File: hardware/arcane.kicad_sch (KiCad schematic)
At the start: 5 parts, among them J1 Conn_01x02, J2 Conn_01x07, SW1 SW_Push, U1 XIAO-nRF52840-SMD

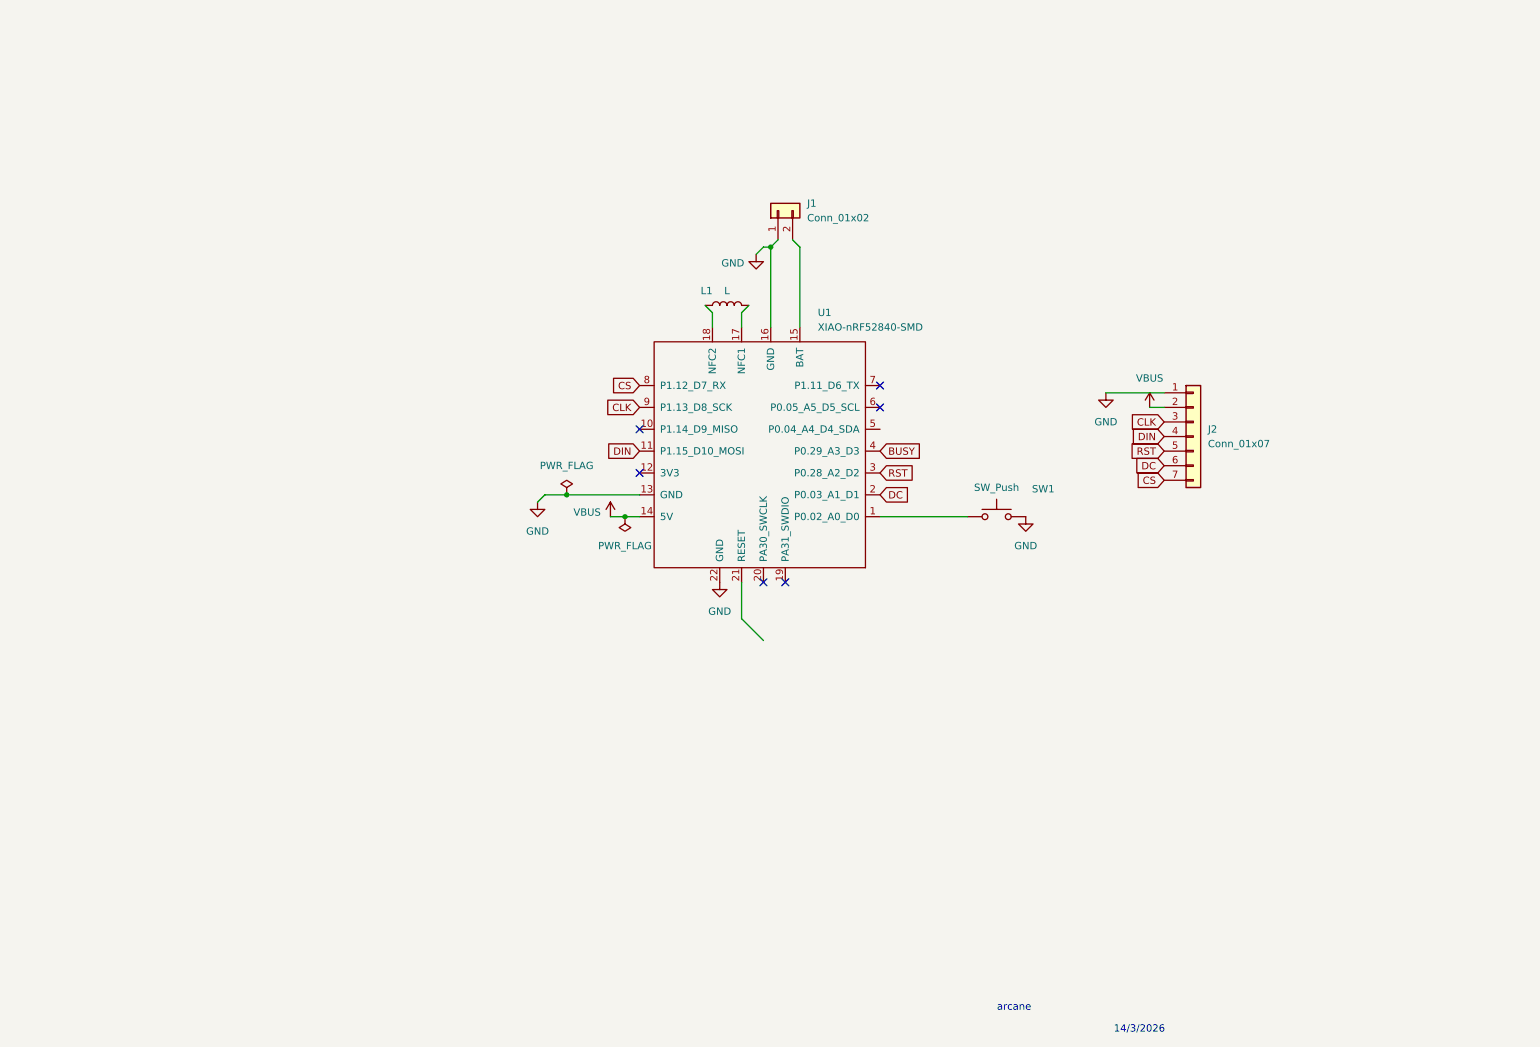
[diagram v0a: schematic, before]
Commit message: migrate to stm32
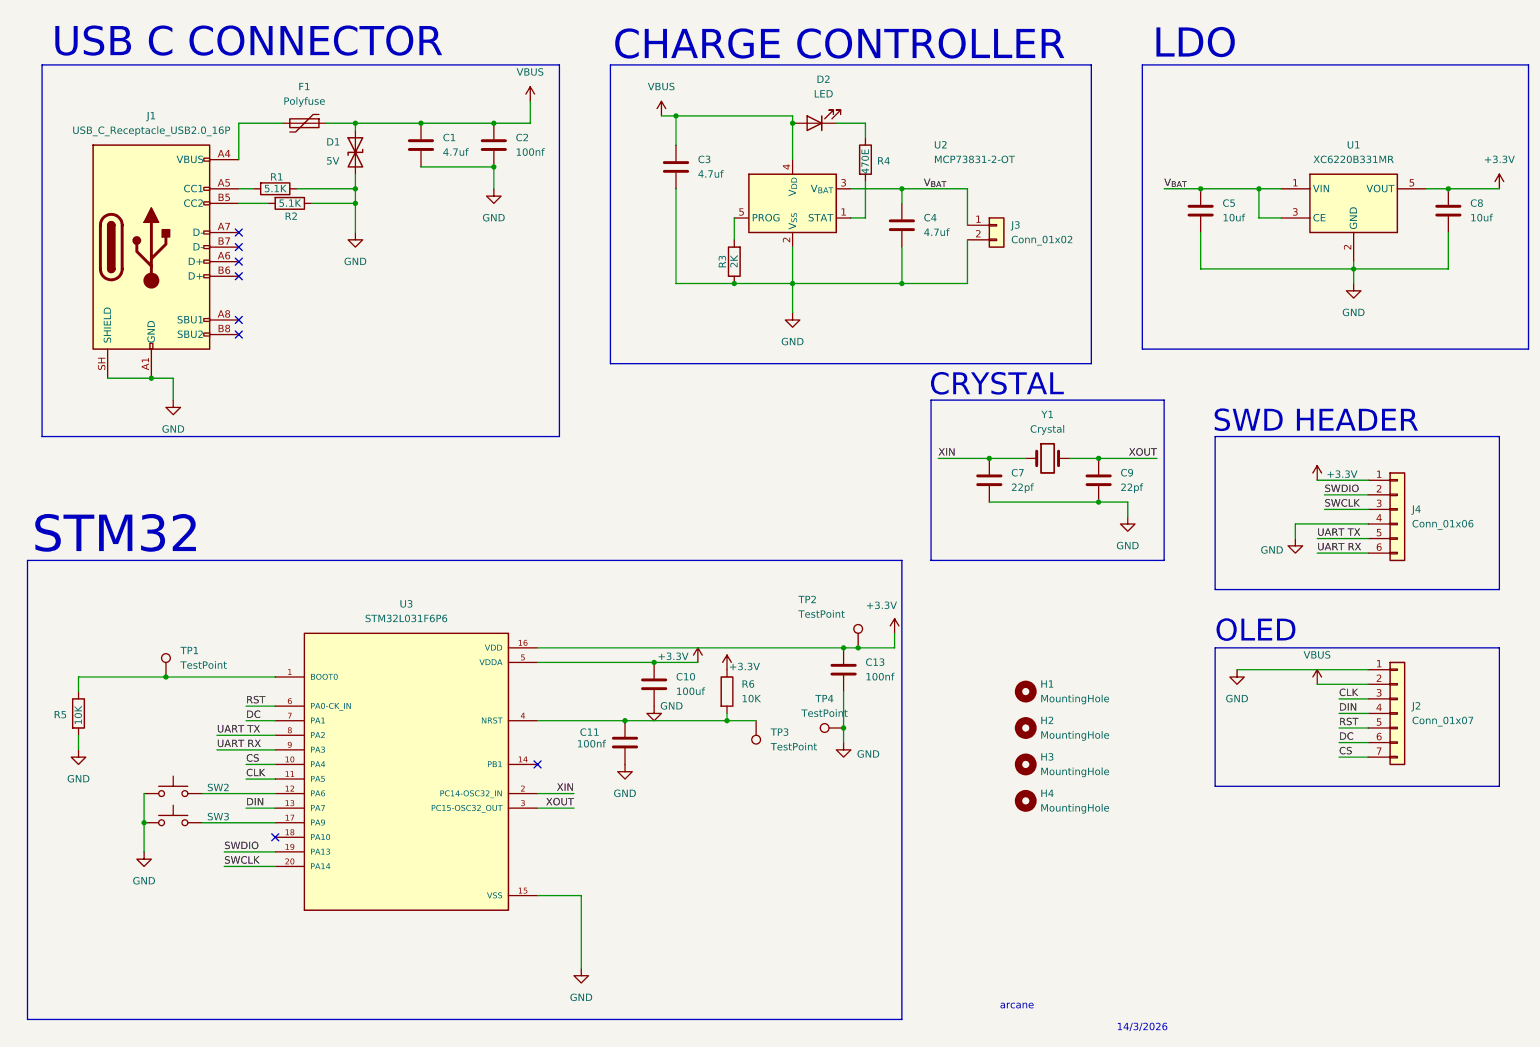
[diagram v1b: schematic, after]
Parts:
- removed J1: Conn_01x02, Connector_JST:JST_PH_B2B-PH-K_1x02_P2.00mm_Vertical, symbol Connector_Generic:Conn_01x02
- removed L1: L, Inductor_SMD:L_6.3x6.3_H3, symbol Device:L
- removed SW1: SW_Push, Button_Switch_THT:SW_PUSH_6mm, symbol Switch:SW_Push
- removed U1: XIAO-nRF52840-SMD, opl:XIAO-nRF52840-SMD, symbol OPL:XIAO-nRF52840-SMD
- added C1, C3, C4: 4.7uf, Capacitor_SMD:C_0603_1608Metric_Pad1.08x0.95mm_HandSolder, symbol Device:C
- added C10: 100uf, Capacitor_SMD:C_0603_1608Metric_Pad1.08x0.95mm_HandSolder, symbol Device:C
- added C11, C13, C2: 100nf, Capacitor_SMD:C_0603_1608Metric_Pad1.08x0.95mm_HandSolder, symbol Device:C
- added C5, C8: 10uf, Capacitor_SMD:C_0603_1608Metric_Pad1.08x0.95mm_HandSolder, symbol Device:C
- added C7, C9: 22pf, Capacitor_SMD:C_0402_1005Metric_Pad0.74x0.62mm_HandSolder, symbol Device:C
- added D1: 5V, Diode_SMD:D_SOD-123, symbol Device:D_TVS
- added D2: LED, LED_SMD:LED_0402_1005Metric_Pad0.77x0.64mm_HandSolder, symbol Device:LED
- added F1: Polyfuse, Fuse:Fuse_0805_2012Metric_Pad1.15x1.40mm_HandSolder, symbol Device:Polyfuse
- added H1, H2, H3, H4: MountingHole, MountingHole:MountingHole_2.2mm_M2, symbol Mechanical:MountingHole
- added J1: USB_C_Receptacle_USB2.0_16P, Connector_USB:USB_C_Receptacle_HRO_TYPE-C-31-M-12, symbol Connector:USB_C_Receptacle_USB2.0_16P
- added J3: Conn_01x02, Connector_JST:JST_XH_S2B-XH-A_1x02_P2.50mm_Horizontal, symbol Connector_Generic:Conn_01x02
- added J4: Conn_01x06, Connector_PinHeader_2.54mm:PinHeader_1x06_P2.54mm_Vertical, symbol Connector_Generic:Conn_01x06
- added R1, R2: 5.1K, Resistor_SMD:R_0603_1608Metric_Pad0.98x0.95mm_HandSolder, symbol Device:R
- added R3: 2K, Resistor_SMD:R_0603_1608Metric_Pad0.98x0.95mm_HandSolder, symbol Device:R
- added R4: 470E, Resistor_SMD:R_0603_1608Metric_Pad0.98x0.95mm_HandSolder, symbol Device:R
- added R5, R6: 10K, Resistor_SMD:R_0603_1608Metric_Pad0.98x0.95mm_HandSolder, symbol Device:R
- added SW2, SW3: SW_Push, Button_Switch_THT:SW_TH_Tactile_Omron_B3F-100x, symbol Switch:SW_Push
- added TP1, TP2, TP3, TP4: TestPoint, TestPoint:TestPoint_Pad_1.0x1.0mm, symbol Connector:TestPoint
- added U1: XC6220B331MR, Package_TO_SOT_SMD:SOT-23-5, symbol Regulator_Linear:XC6220B331MR
- added U2: MCP73831-2-OT, Package_TO_SOT_SMD:SOT-23-5, symbol Battery_Management:MCP73831-2-OT
- added U3: STM32L031F6P6, STM32:SOP65P640X120-20N, symbol STM32:STM32L031F6P6
- added Y1: Crystal, Crystal:Crystal_SMD_3215-2Pin_3.2x1.5mm, symbol Device:Crystal
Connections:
- net CLK: now also U3.11 (PA5)
- net CS: now also U3.10 (PA4)
- net DC: now also U3.7 (PA1)
- net DIN: now also U3.13 (PA7)
- net GND: now also C1.2, C10.2, C11.2, C13.2, C2.2, C3.2, C4.2, C5.2, C7.2, C8.2, C9.2, D1.2 (A2), J1.A1 (GND), J1.A12 (GND), J1.B1 (GND), J1.B12 (GND), J1.SH (SHIELD), J3.2 (Pin_2), J4.4 (Pin_4), R1.1, R2.1, R3.1, R5.2, SW2.1, SW3.1, TP4.1, U1.2 (GND), U2.2 (V_{SS}), U3.15 (VSS)
- net RST: now also U3.6 (PA0-CK_IN)
- net VBUS: now also C1.1, C2.1, C3.1, D1.1 (A1), D2.2 (A), F1.1, U2.4 (V_{DD})
- new net: J1.A5 (CC1), R1.2
- new net: SW3.2, U3.17 (PA9)
- new net: R5.1, TP1.1, U3.1 (BOOT0)
- new net: SW2.2, U3.12 (PA6)
- new net: C11.1, R6.2, TP3.1, U3.4 (NRST)
- new net: D2.1 (K), R4.1
- new net: R4.2, U2.1 (STAT)
- new net: J1.B5 (CC2), R2.2
- new net: F1.2, J1.A4 (VBUS), J1.A9 (VBUS), J1.B4 (VBUS), J1.B9 (VBUS)
- new net: R3.2, U2.5 (PROG)
- new net +3.3V: C10.1, C13.1, C8.1, J4.1 (Pin_1), R6.1, TP2.1, U1.5 (VOUT), U3.16 (VDD), U3.5 (VDDA)
- new net SWCLK: J4.3 (Pin_3), U3.20 (PA14)
- new net SWDIO: J4.2 (Pin_2), U3.19 (PA13)
- new net UART RX: J4.6 (Pin_6), U3.9 (PA3)
- new net UART TX: J4.5 (Pin_5), U3.8 (PA2)
- new net V_{BAT}: C4.1, C5.1, J3.1 (Pin_1), U1.1 (VIN), U1.3 (CE), U2.3 (V_{BAT})
- new net XIN: C7.1, U3.2 (PC14-OSC32_IN), Y1.1
- new net XOUT: C9.1, U3.3 (PC15-OSC32_OUT), Y1.2
- no-connect marks 6 -> 8
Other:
- note added: "CHARGE CONTROLLER"
- note added: "CRYSTAL"
- note added: "LDO"
- note added: "OLED"
- note added: "STM32"
- note added: "SWD HEADER"
- note added: "USB C CONNECTOR"
- moved on the sheet: J2

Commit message: update: zine, firmware and gerber
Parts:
- SW2, SW3: footprint Button_Switch_THT:SW_TH_Tactile_Omron_B3F-100x -> Button_Switch_SMD:SW_SPST_TL3342
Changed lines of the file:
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@@
 		)
 		(instances
-			(project "arcane_panelized"
+			(project "arcane"
 				(path "/1f77d9ea-a7f8-4bd5-9b2a-3d0e599b2c25"
 					(reference "R1")
@@
 		)
 		(instances
-			(project "arcane_panelized"
+			(project "arcane"
 				(path "/1f77d9ea-a7f8-4bd5-9b2a-3d0e599b2c25"
 					(reference "C9")
@@
 			)
 		)
-		(property "Footprint" "Button_Switch_THT:SW_TH_Tactile_Omron_B3F-100x"
+		(property "Footprint" "Button_Switch_SMD:SW_SPST_TL3342"
 			(at 43.18 152.4 0)
 			(hide yes)
@@
 		)
 		(instances
-			(project "arcane_panelized"
+			(project "arcane"
 				(path "/1f77d9ea-a7f8-4bd5-9b2a-3d0e599b2c25"
 					(reference "SW3")
@@
 		)
 		(instances
-			(project "arcane_panelized"
+			(project "arcane"
 				(path "/1f77d9ea-a7f8-4bd5-9b2a-3d0e599b2c25"
 					(reference "U3")
@@
 		)
 		(instances
-			(project "arcane_panelized"
+			(project "arcane"
 				(path "/1f77d9ea-a7f8-4bd5-9b2a-3d0e599b2c25"
 					(reference "R4")
@@
 		)
 		(instances
-			(project "arcane_panelized"
+			(project "arcane"
 				(path "/1f77d9ea-a7f8-4bd5-9b2a-3d0e599b2c25"
 					(reference "#PWR022")
@@
 		)
 		(instances
-			(project "arcane_panelized"
+			(project "arcane"
 				(path "/1f77d9ea-a7f8-4bd5-9b2a-3d0e599b2c25"
 					(reference "H4")
@@
 		)
 		(instances
-			(project "arcane_panelized"
+			(project "arcane"
 				(path "/1f77d9ea-a7f8-4bd5-9b2a-3d0e599b2c25"
 					(reference "#PWR012")
@@
 		)
 		(instances
-			(project "arcane_panelized"
+			(project "arcane"
 				(path "/1f77d9ea-a7f8-4bd5-9b2a-3d0e599b2c25"
 					(reference "H1")
@@
 		)
 		(instances
-			(project "arcane_panelized"
+			(project "arcane"
 				(path "/1f77d9ea-a7f8-4bd5-9b2a-3d0e599b2c25"
 					(reference "#PWR016")
@@
 		)
 		(instances
-			(project "arcane_panelized"
+			(project "arcane"
 				(path "/1f77d9ea-a7f8-4bd5-9b2a-3d0e599b2c25"
 					(reference "C11")
@@
 		)
 		(instances
-			(project "arcane_panelized"
+			(project "arcane"
 				(path "/1f77d9ea-a7f8-4bd5-9b2a-3d0e599b2c25"
 					(reference "TP1")
@@
 		)
 		(instances
-			(project "arcane_panelized"
+			(project "arcane"
 				(path "/1f77d9ea-a7f8-4bd5-9b2a-3d0e599b2c25"
 					(reference "#PWR01")
@@
 		)
 		(instances
-			(project "arcane_panelized"
+			(project "arcane"
 				(path "/1f77d9ea-a7f8-4bd5-9b2a-3d0e599b2c25"
 					(reference "C7")
@@
 		)
 		(instances
-			(project "arcane_panelized"
+			(project "arcane"
 				(path "/1f77d9ea-a7f8-4bd5-9b2a-3d0e599b2c25"
 					(reference "TP3")
@@
 		)
 		(instances
-			(project "arcane_panelized"
+			(project "arcane"
 				(path "/1f77d9ea-a7f8-4bd5-9b2a-3d0e599b2c25"
 					(reference "#PWR06")
@@
 		)
 		(instances
-			(project "arcane_panelized"
+			(project "arcane"
 				(path "/1f77d9ea-a7f8-4bd5-9b2a-3d0e599b2c25"
 					(reference "U1")
@@
 		)
 		(instances
-			(project "arcane_panelized"
+			(project "arcane"
 				(path "/1f77d9ea-a7f8-4bd5-9b2a-3d0e599b2c25"
 					(reference "R2")
@@
 		)
 		(instances
-			(project "arcane_panelized"
+			(project "arcane"
 				(path "/1f77d9ea-a7f8-4bd5-9b2a-3d0e599b2c25"
 					(reference "#PWR015")
@@
 		)
 		(instances
-			(project "arcane_panelized"
+			(project "arcane"
 				(path "/1f77d9ea-a7f8-4bd5-9b2a-3d0e599b2c25"
 					(reference "R6")
@@
 		)
 		(instances
-			(project "arcane_panelized"
+			(project "arcane"
 				(path "/1f77d9ea-a7f8-4bd5-9b2a-3d0e599b2c25"
 					(reference "J3")
@@
 		)
 		(instances
-			(project "arcane_panelized"
+			(project "arcane"
 				(path "/1f77d9ea-a7f8-4bd5-9b2a-3d0e599b2c25"
 					(reference "#PWR017")
@@
 		)
 		(instances
-			(project "arcane_panelized"
+			(project "arcane"
 				(path "/1f77d9ea-a7f8-4bd5-9b2a-3d0e599b2c25"
 					(reference "C2")
@@
 		)
 		(instances
-			(project "arcane_panelized"
+			(project "arcane"
 				(path "/1f77d9ea-a7f8-4bd5-9b2a-3d0e599b2c25"
 					(reference "#PWR020")
@@
 		)
 		(instances
-			(project "arcane_panelized"
+			(project "arcane"
 				(path "/1f77d9ea-a7f8-4bd5-9b2a-3d0e599b2c25"
 					(reference "F1")
@@
 		)
 		(instances
-			(project "arcane_panelized"
+			(project "arcane"
 				(path "/1f77d9ea-a7f8-4bd5-9b2a-3d0e599b2c25"
 					(reference "#PWR02")
@@
 		)
 		(instances
-			(project "arcane_panelized"
+			(project "arcane"
 				(path "/1f77d9ea-a7f8-4bd5-9b2a-3d0e599b2c25"
 					(reference "C13")
@@
 		)
 		(instances
-			(project "arcane_panelized"
+			(project "arcane"
 				(path "/1f77d9ea-a7f8-4bd5-9b2a-3d0e599b2c25"
 					(reference "TP2")
@@
 			)
 		)
-		(property "Footprint" "Button_Switch_THT:SW_TH_Tactile_Omron_B3F-100x"
+		(property "Footprint" "Button_Switch_SMD:SW_SPST_TL3342"
 			(at 43.18 147.32 0)
 			(hide yes)
@@
 		)
 		(instances
-			(project "arcane_panelized"
+			(project "arcane"
 				(path "/1f77d9ea-a7f8-4bd5-9b2a-3d0e599b2c25"
 					(reference "SW2")
@@
 		)
 		(instances
-			(project "arcane_panelized"
+			(project "arcane"
 				(path "/1f77d9ea-a7f8-4bd5-9b2a-3d0e599b2c25"
 					(reference "#PWR05")
@@
 		)
 		(instances
-			(project "arcane_panelized"
+			(project "arcane"
 				(path "/1f77d9ea-a7f8-4bd5-9b2a-3d0e599b2c25"
 					(reference "R5")
@@
 		)
 		(instances
-			(project "arcane_panelized"
+			(project "arcane"
 				(path "/1f77d9ea-a7f8-4bd5-9b2a-3d0e599b2c25"
 					(reference "#PWR07")
@@
 		)
 		(instances
-			(project "arcane_panelized"
+			(project "arcane"
 				(path "/1f77d9ea-a7f8-4bd5-9b2a-3d0e599b2c25"
 					(reference "C10")
@@
 		)
 		(instances
-			(project "arcane_panelized"
+			(project "arcane"
 				(path "/1f77d9ea-a7f8-4bd5-9b2a-3d0e599b2c25"
 					(reference "C3")
@@
 		)
 		(instances
-			(project "arcane_panelized"
+			(project "arcane"
 				(path "/1f77d9ea-a7f8-4bd5-9b2a-3d0e599b2c25"
 					(reference "#PWR021")
@@
 		)
 		(instances
-			(project "arcane_panelized"
+			(project "arcane"
 				(path "/1f77d9ea-a7f8-4bd5-9b2a-3d0e599b2c25"
 					(reference "H2")
@@
 		)
 		(instances
-			(project "arcane_panelized"
+			(project "arcane"
 				(path "/1f77d9ea-a7f8-4bd5-9b2a-3d0e599b2c25"
 					(reference "D1")
@@
 		)
 		(instances
-			(project "arcane_panelized"
+			(project "arcane"
 				(path "/1f77d9ea-a7f8-4bd5-9b2a-3d0e599b2c25"
 					(reference "U2")
@@
 		)
 		(instances
-			(project "arcane_panelized"
+			(project "arcane"
 				(path "/1f77d9ea-a7f8-4bd5-9b2a-3d0e599b2c25"
 					(reference "C1")
@@
 		)
 		(instances
-			(project "arcane_panelized"
+			(project "arcane"
 				(path "/1f77d9ea-a7f8-4bd5-9b2a-3d0e599b2c25"
 					(reference "H3")
@@
 		)
 		(instances
-			(project "arcane_panelized"
+			(project "arcane"
 				(path "/1f77d9ea-a7f8-4bd5-9b2a-3d0e599b2c25"
 					(reference "Y1")
@@
 		)
 		(instances
-			(project "arcane_panelized"
+			(project "arcane"
 				(path "/1f77d9ea-a7f8-4bd5-9b2a-3d0e599b2c25"
 					(reference "C4")
@@
 		)
 		(instances
-			(project "arcane_panelized"
+			(project "arcane"
 				(path "/1f77d9ea-a7f8-4bd5-9b2a-3d0e599b2c25"
 					(reference "#PWR018")
@@
 		)
 		(instances
-			(project "arcane_panelized"
+			(project "arcane"
 				(path "/1f77d9ea-a7f8-4bd5-9b2a-3d0e599b2c25"
 					(reference "C5")
@@
 		)
 		(instances
-			(project "arcane_panelized"
+			(project "arcane"
 				(path "/1f77d9ea-a7f8-4bd5-9b2a-3d0e599b2c25"
 					(reference "D2")
@@
 		)
 		(instances
-			(project "arcane_panelized"
+			(project "arcane"
 				(path "/1f77d9ea-a7f8-4bd5-9b2a-3d0e599b2c25"
 					(reference "#PWR019")
@@
 		)
 		(instances
-			(project "arcane_panelized"
+			(project "arcane"
 				(path "/1f77d9ea-a7f8-4bd5-9b2a-3d0e599b2c25"
 					(reference "#PWR023")
@@
 		)
 		(instances
-			(project "arcane_panelized"
+			(project "arcane"
 				(path "/1f77d9ea-a7f8-4bd5-9b2a-3d0e599b2c25"
 					(reference "C8")
@@
 		)
 		(instances
-			(project "arcane_panelized"
+			(project "arcane"
 				(path "/1f77d9ea-a7f8-4bd5-9b2a-3d0e599b2c25"
 					(reference "R3")
@@
 		)
 		(instances
-			(project "arcane_panelized"
+			(project "arcane"
 				(path "/1f77d9ea-a7f8-4bd5-9b2a-3d0e599b2c25"
 					(reference "#PWR04")
@@
 		)
 		(instances
-			(project "arcane_panelized"
+			(project "arcane"
 				(path "/1f77d9ea-a7f8-4bd5-9b2a-3d0e599b2c25"
 					(reference "#PWR010")
@@
 		)
 		(instances
-			(project "arcane_panelized"
+			(project "arcane"
 				(path "/1f77d9ea-a7f8-4bd5-9b2a-3d0e599b2c25"
 					(reference "#PWR08")
@@
 		)
 		(instances
-			(project "arcane_panelized"
+			(project "arcane"
 				(path "/1f77d9ea-a7f8-4bd5-9b2a-3d0e599b2c25"
 					(reference "#PWR014")
@@
 		)
 		(instances
-			(project "arcane_panelized"
+			(project "arcane"
 				(path "/1f77d9ea-a7f8-4bd5-9b2a-3d0e599b2c25"
 					(reference "J1")
@@
 		)
 		(instances
-			(project "arcane_panelized"
+			(project "arcane"
 				(path "/1f77d9ea-a7f8-4bd5-9b2a-3d0e599b2c25"
 					(reference "#PWR011")
@@
 		)
 		(instances
-			(project "arcane_panelized"
+			(project "arcane"
 				(path "/1f77d9ea-a7f8-4bd5-9b2a-3d0e599b2c25"
 					(reference "TP4")
@@
 		)
 		(instances
-			(project "arcane_panelized"
+			(project "arcane"
 				(path "/1f77d9ea-a7f8-4bd5-9b2a-3d0e599b2c25"
 					(reference "J4")
@@
 		)
 		(instances
-			(project "arcane_panelized"
+			(project "arcane"
 				(path "/1f77d9ea-a7f8-4bd5-9b2a-3d0e599b2c25"
 					(reference "#PWR03")
@@
 		)
 		(instances
-			(project "arcane_panelized"
+			(project "arcane"
 				(path "/1f77d9ea-a7f8-4bd5-9b2a-3d0e599b2c25"
 					(reference "J2")
@@
 		)
 		(instances
-			(project "arcane_panelized"
+			(project "arcane"
 				(path "/1f77d9ea-a7f8-4bd5-9b2a-3d0e599b2c25"
 					(reference "#PWR013")
